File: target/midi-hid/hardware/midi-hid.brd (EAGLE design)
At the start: 100 x 80 mm, 0 parts

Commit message: midi-hid hardware interim drop
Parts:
- added C1, C2: (no value), rcl:C0805
- added D1, D10, D11, D12, D13, D14, D15, D16, D17, D18, D19, D2, D20, D21, D22, D23, D24, D3, D4, D5, D6, D7, D8, D9: (no value), diode:SOD80C
- added IC1: MEGA48/88/168-AU, avr-7:TQFP32-08
- added PAD1, PAD10, PAD11, PAD12, PAD13, PAD14, PAD15, PAD16, PAD17, PAD18, PAD19, PAD2, PAD20, PAD21, PAD22, PAD23, PAD24, PAD25, PAD26, PAD27, PAD28, PAD29, PAD3, PAD30, PAD31, PAD32, PAD33, PAD34, PAD35, PAD36, PAD37, PAD38, PAD39, PAD4, PAD40, PAD41, PAD42, PAD43, PAD44, PAD45, PAD46, PAD47, PAD48, PAD49, PAD5, PAD50, PAD51, PAD52, PAD53, PAD54, PAD55, PAD56, PAD6, PAD7, PAD8, PAD9: (no value), wirepad:1,6/0,8
- added Q1: (no value), crystal:HC49/S
- added R1, R10, R11, R12, R13, R14, R15, R16, R17, R18, R19, R2, R20, R21, R22, R23, R24, R25, R26, R27, R28, R29, R3, R30, R31, R32, R4, R5, R6, R7, R8, R9: (no value), rcl:R0805
- added S1, S2, S3, S4: (no value), switch-omron:B3F-40XX
- added SW1, SW2, SW3, SW4: EC12E_SW, switch-alps:ALPS_EC12E_SW
- added T1, T2, T3, T4: (no value), transistor:SOT23-BEC
- added U$1, U$2, U$3, U$4, U$6, U$7, U$8, U$9: (no value), holes:3,0
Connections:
- new net ADC6: IC1.19
- new net ADC7: IC1.22
- new net BUTROW0: IC1.15
- new net BUTROW1: IC1.16
- new net BUTROW2: IC1.17
- new net COLUMN0: IC1.23
- new net COLUMN1: IC1.24
- new net COLUMN2: IC1.25
- new net COLUMN3: IC1.26
- new net ENCROWA: IC1.12
- new net ENCROWB: IC1.13
- new net ENCROWS: IC1.14
- new net GND: C1.2, C2.2, IC1.21, IC1.3, IC1.5, PAD11.1, PAD17.1, PAD23.1, PAD29.1, PAD35.1, PAD41.1, PAD47.1, PAD53.1
- new net INTOUT: IC1.31
- new net LEDROW0: IC1.32
- new net LEDROW1: IC1.1
- new net LEDROW2: IC1.2
- new net LEDROW3: IC1.9, R3.1
- new net LEDROW4: IC1.10
- new net LEDROW5: IC1.11
- new net LEDROWB: IC1.30
- new net N$10: SW2.D
- new net N$11: D13.C, SW3.B
- new net N$12: D14.C, SW3.A
- new net N$14: D15.C, SW4.B
- new net N$15: D16.C, SW4.A
- new net N$17: SW4.C
- new net N$18: SW4.D
- new net N$19: SW3.C
- new net N$20: SW3.D
- new net N$21: C1.1, IC1.7, Q1.1
- new net N$22: C2.1, IC1.8, Q1.2
- new net N$23: R29.2, T1.B
- new net N$24: PAD36.1, R1.2
- new net N$25: PAD37.1, R2.2
- new net N$26: PAD38.1, R3.2
- new net N$27: R30.2, T2.B
- new net N$28: PAD42.1, R4.2
- new net N$29: PAD43.1, R5.2
- new net N$30: PAD44.1, R6.2
- new net N$31: R31.2, T3.B
- new net N$32: PAD48.1, R7.2
- new net N$33: PAD49.1, R8.2
- new net N$34: PAD50.1, R9.2
- new net N$35: R32.2, T4.B
- new net N$36: PAD54.1, R10.2
- new net N$37: PAD55.1, R11.2
- new net N$38: PAD56.1, R12.2
- new net N$39: PAD33.1
- new net N$4: SW1.C
- new net N$40: D3.A, PAD34.1
- new net N$41: PAD39.1
- new net N$42: D7.A, PAD40.1
- new net N$43: PAD45.1
- new net N$44: D4.A, PAD46.1
- new net N$45: PAD51.1
- new net N$46: D8.A, PAD52.1
- new net N$47: PAD14.1, R15.2
- new net N$48: PAD13.1, R14.2
- new net N$49: PAD12.1, R13.2
- new net N$5: SW1.D
- new net N$51: PAD20.1, R18.2
- new net N$52: PAD19.1, R17.2
- new net N$53: PAD18.1, R16.2
- new net N$54: R2.1
- new net N$55: R1.1
- new net N$56: PAD24.1, R19.2
- new net N$57: PAD25.1, R20.2
- new net N$58: PAD26.1, R21.2
- new net N$59: PAD32.1, R24.2
- new net N$6: D11.C, SW2.B
- new net N$60: PAD31.1, R23.2
- new net N$61: PAD30.1, R22.2
- new net N$62: R7.1
- new net N$63: PAD9.1
- new net N$64: D1.A, PAD10.1
- new net N$65: PAD15.1
- new net N$66: D5.A, PAD16.1
- new net N$67: PAD21.1
- new net N$68: D2.A, PAD22.1
- new net N$69: PAD27.1
- new net N$7: D12.C, SW2.A
- new net N$70: D6.A, PAD28.1
- new net N$71: PAD2.1
- new net N$72: PAD1.1, R28.2
- new net N$73: PAD4.1
- new net N$74: PAD3.1, R27.2
- new net N$75: PAD6.1
- new net N$76: PAD5.1, R26.2
- new net N$77: PAD8.1
- new net N$78: PAD7.1, R25.2
- new net N$79: R8.1
- new net N$80: R9.1
- new net N$81: R12.1
- new net N$82: R11.1
- new net N$83: R10.1
- new net N$84: R6.1
- new net N$85: R5.1
- new net N$86: R4.1
- new net N$9: SW2.C
- new net RESET: IC1.29
- new net SCL: IC1.28
- new net SDA: IC1.27
- new net VCC: IC1.18, IC1.20, IC1.4, IC1.6
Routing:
- net LEDROW3: track 0.00 -> 51.6 mm
- net GND: track 0.00 -> 25.2 mm
- net N$22: track 0.00 -> 6.68 mm
- net N$21: track 0.00 -> 5.02 mm

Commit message: midi-hid hardware interim drop
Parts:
- added U$5: (no value), holes:3,0
- moved R29 27.2 mm to (27.8, 27.0), turned to 90 degrees
- moved R30 27.2 mm to (46.8, 27.0), turned to 90 degrees
- moved R31 26.8 mm to (65.8, 27.0), turned to 90 degrees
- moved R32 26.8 mm to (84.8, 27.0), turned to 90 degrees
- moved T1 26.2 mm to (30.8, 27.0), turned to 270 degrees
- moved T2 26.2 mm to (49.8, 27.0), turned to 270 degrees
- moved T3 26.2 mm to (68.8, 27.0), turned to 270 degrees
- moved T4 26.2 mm to (87.8, 27.0), turned to 270 degrees
- moved D17 19.6 mm to (15.5, 80.5), turned to 0 degrees
- moved D18 19.6 mm to (34.5, 80.5), turned to 0 degrees
- moved D19 19.6 mm to (53.5, 80.5), turned to 0 degrees
- moved D20 19.6 mm to (72.5, 80.5), turned to 0 degrees
- moved D10 16.5 mm to (24.0, 91.5), turned to 270 degrees
- moved D12 16.5 mm to (43.0, 91.5), turned to 270 degrees
- moved D14 16.5 mm to (62.0, 91.5), turned to 270 degrees
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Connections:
- new net C0: D1.C, D3.C, SW1.C, SW1.D, T1.C
- new net C1: D5.C, D7.C, SW2.C, SW2.D, T2.C
- new net C2: D2.C, D4.C, SW3.C, SW3.D, T3.C
- new net C3: D6.C, D8.C, SW4.C, SW4.D, T4.C
- new net N$1: D9.C, SW1.B
- new net N$13: D19.C, SW3.E
- new net N$16: D20.C, SW4.E
- new net N$2: D10.C, SW1.A
- new net N$3: D17.C, SW1.E
- new net N$50: R24.1
- new net N$8: D18.C, SW2.E
- new net N$87: R16.1
- new net N$91: R31.1
- new net N$95: R32.1
- net COLUMN0: now also R29.1
- net COLUMN1: now also R30.1
- net ENCROWA: now also D10.A, D12.A, D14.A, D16.A
- net ENCROWB: now also D11.A, D13.A, D15.A, D9.A
- net ENCROWS: now also D17.A, D18.A, D19.A, D20.A
- net GND: now also T1.E, T2.E, T3.E, T4.E
- net LEDROW4: now also R2.1
- net LEDROW5: now also R1.1
- net N$10: now also R19.1; no longer SW2.D
- net N$17: now also R20.1; no longer SW4.C
- net N$18: now also R21.1; no longer SW4.D
- net N$19: now also R22.1; no longer SW3.C
- net N$20: now also R23.1; no longer SW3.D
- net N$4: now also R13.1; no longer SW1.C
- net N$5: now also R14.1; no longer SW1.D
- net N$54: now also R18.1; no longer R2.1
- net N$55: now also R17.1; no longer R1.1
- net N$9: now also R15.1; no longer SW2.C
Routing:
- net ENCROWB: track 0.00 -> 138.9 mm
- net ENCROWA: track 0.00 -> 134.2 mm
- net ENCROWS: track 0.00 -> 134.1 mm
- net C1: track 0.00 -> 95.4 mm
- net C0: track 0.00 -> 92.5 mm
- net C3: track 0.00 -> 92.5 mm
- net C2: track 0.00 -> 92.5 mm
- net LEDROW3: track 51.6 -> 0.77 mm
- net N$6: track 0.00 -> 3.30 mm
- net N$14: track 0.00 -> 3.30 mm
- net N$11: track 0.00 -> 3.30 mm
- net N$1: track 0.00 -> 3.30 mm
- net N$70: track 0.00 -> 2.30 mm
- net N$68: track 0.00 -> 2.30 mm
- net N$66: track 0.00 -> 2.30 mm
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
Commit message: routing midi-hid
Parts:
- added C3, C4: (no value), rcl:C0805
- added C5: (no value), rcl:E2,5-6
- added PAD57, PAD58, PAD59: WIREPAD1,6/0,8, wirepad:1,6/0,8
- added R33, R34: (no value), rcl:0207/10
- added SV1: (no value), con-lstb:MA05-1
- added USBCONN: MICRO-USB, microusb:MICRO-USB
- moved R12 6.95 mm to (75.5, 77.0), turned to 0 degrees
- moved R15 6.95 mm to (18.5, 52.0), turned to 0 degrees
- moved R18 6.95 mm to (37.5, 52.0), turned to 0 degrees
- moved R24 6.95 mm to (75.5, 52.0), turned to 0 degrees
- moved R3 6.95 mm to (18.5, 77.0), turned to 0 degrees
- moved R6 6.95 mm to (37.5, 77.0), turned to 0 degrees
- moved R9 6.95 mm to (56.5, 77.0), turned to 0 degrees
- moved R11 4.27 mm to (75.5, 75.0), turned to 0 degrees
- moved R14 4.27 mm to (18.5, 50.0), turned to 0 degrees
- moved R17 4.27 mm to (37.5, 50.0), turned to 0 degrees
- moved R2 4.27 mm to (18.5, 75.0), turned to 0 degrees
- moved R23 4.27 mm to (75.5, 50.0), turned to 0 degrees
- moved R5 4.27 mm to (37.5, 75.0), turned to 0 degrees
- moved R8 4.27 mm to (56.5, 75.0), turned to 0 degrees
- moved R25 3.61 mm to (81.5, 20.0), turned to 180 degrees
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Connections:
- removed net N$10: R19.1
- removed net N$17: R20.1
- removed net N$18: R21.1
- removed net N$19: R22.1
- removed net N$20: R23.1
- removed net N$39: PAD33.1
- removed net N$4: R13.1
- removed net N$41: PAD39.1
- removed net N$43: PAD45.1
- removed net N$45: PAD51.1
- removed net N$5: R14.1
- removed net N$50: R24.1
- removed net N$54: R18.1
- removed net N$55: R17.1
- removed net N$62: R7.1
- removed net N$63: PAD9.1
- removed net N$65: PAD15.1
- removed net N$67: PAD21.1
- removed net N$69: PAD27.1
- removed net N$71: PAD2.1
- removed net N$73: PAD4.1
- removed net N$75: PAD6.1
- removed net N$77: PAD8.1
- removed net N$79: R8.1
- removed net N$80: R9.1
- removed net N$81: R12.1
- removed net N$82: R11.1
- removed net N$83: R10.1
- removed net N$84: R6.1
- removed net N$85: R5.1
- removed net N$86: R4.1
- removed net N$87: R16.1
- removed net N$9: R15.1
- removed net N$95: R32.1
- new net DM: USBCONN.2
- new net DP: USBCONN.3
- new net ID: USBCONN.4
- new net N$88: D22.C, S2.2
- new net N$89: D21.C, S1.2
- new net N$90: D23.C, S3.2
- net ADC6: now also PAD58.1
- net ADC7: now also PAD59.1
- net BUTROW0: now also PAD33.1, PAD39.1, PAD45.1, PAD51.1
- net BUTROW1: now also PAD15.1, PAD21.1, PAD27.1, PAD9.1
- net BUTROW2: now also D21.A, D22.A, D23.A, D24.A
- net C0: now also PAD2.1, S1.4
- net C1: now also PAD4.1, S2.4
- net C2: now also PAD6.1, S3.4
- net C3: now also PAD8.1, S4.4
- net COLUMN2: now also R31.1
- net COLUMN3: now also R32.1
- net GND: now also C3.2, C4.2, C5.-, SV1.2, USBCONN.5, USBCONN.GND1, USBCONN.GND2
- net INTOUT: now also SV1.5
- net LEDROW0: now also R15.1, R18.1, R21.1, R24.1
- net LEDROW1: now also R14.1, R17.1, R20.1, R23.1
- net LEDROW2: now also R13.1, R16.1, R19.1, R22.1
- net LEDROW3: now also R12.1, R6.1, R9.1
- net LEDROW4: now also R11.1, R5.1, R8.1
- net LEDROW5: now also R10.1, R4.1, R7.1
- net LEDROWB: now also R25.1, R26.1, R27.1, R28.1
- net N$91: now also D24.C, S4.2; no longer R31.1
- net RESET: now also PAD57.1
- net SCL: now also SV1.3
- net SDA: now also SV1.4
- net VCC: now also C3.1, C4.1, C5.+, SV1.1, USBCONN.1
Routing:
- net GND: track 25.2 -> 580.6 mm, vias 0 -> 4
- net VCC: track 0.00 -> 349.0 mm, vias 0 -> 1
- net INTOUT: track 0.00 -> 131.6 mm
- net LEDROW3: track 0.77 -> 122.5 mm, vias 0 -> 5
- net LEDROW4: track 0.78 -> 119.3 mm, vias 0 -> 5
- net LEDROW0: track 0.00 -> 118.2 mm, vias 0 -> 5
- net LEDROW5: track 0.78 -> 116.2 mm, vias 0 -> 5
- net LEDROW1: track 0.00 -> 110.1 mm, vias 0 -> 5
- net LEDROW2: track 0.00 -> 108.0 mm, vias 0 -> 5
- net SDA: track 0.00 -> 97.7 mm, vias 0 -> 2
- net SCL: track 0.00 -> 94.9 mm, vias 0 -> 2
- net BUTROW2: track 0.00 -> 93.6 mm, vias 0 -> 5
- net LEDROWB: track 0.00 -> 93.3 mm, vias 0 -> 5
- net BUTROW0: track 0.00 -> 93.2 mm
- net BUTROW1: track 0.00 -> 78.3 mm
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
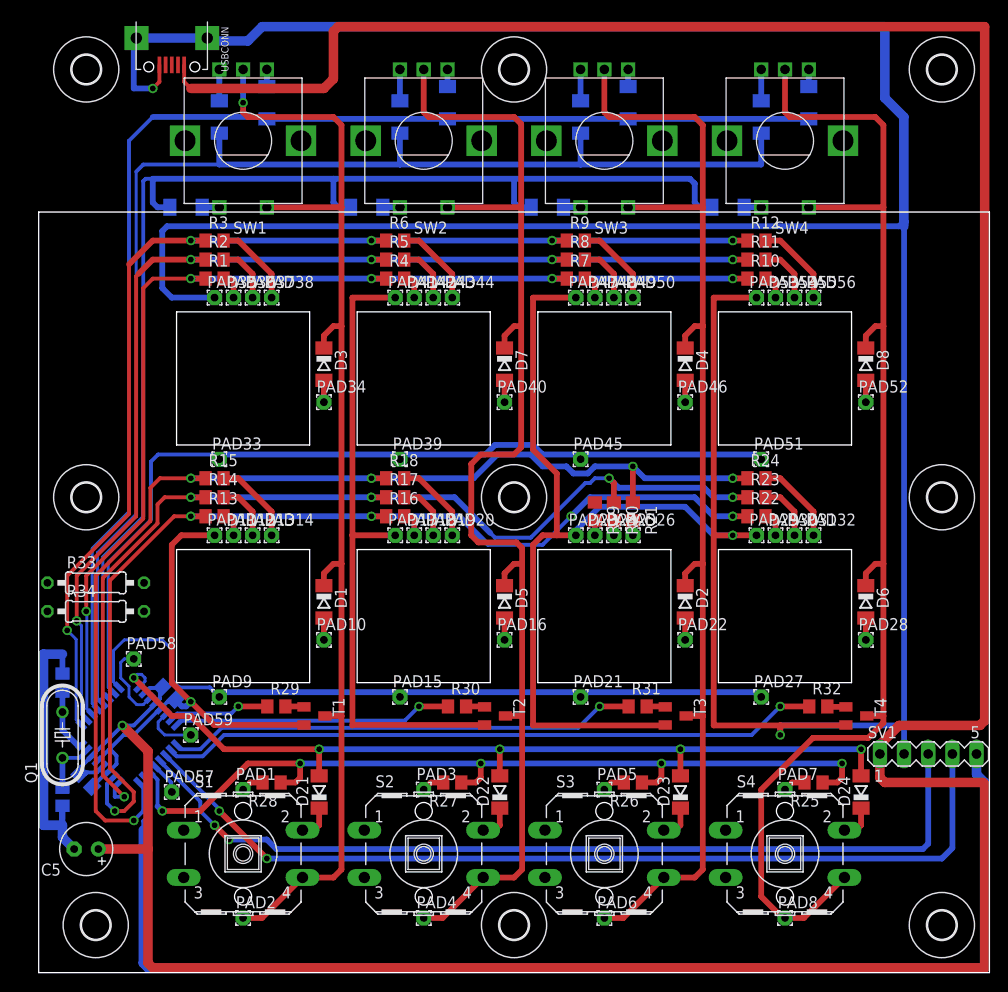
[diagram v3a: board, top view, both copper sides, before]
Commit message: midi-hid hardware
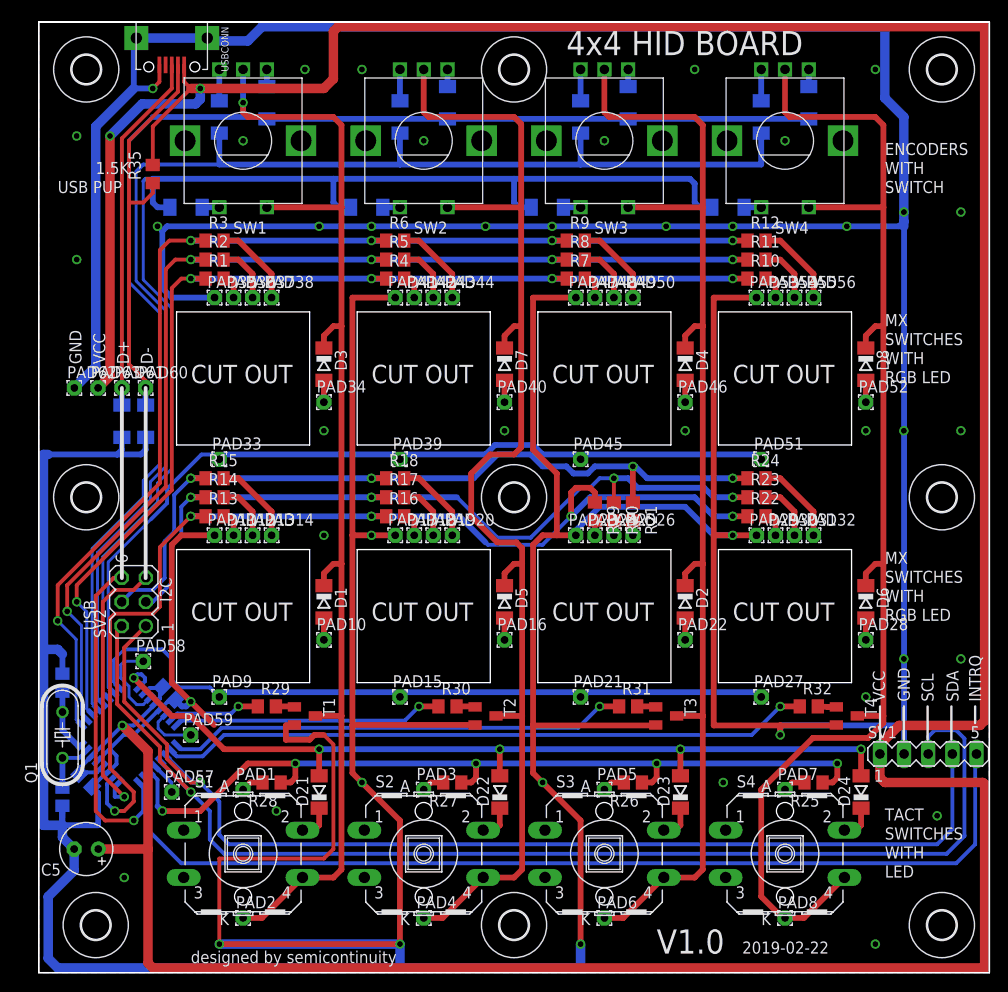
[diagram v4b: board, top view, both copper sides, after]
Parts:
- removed R33, R34: (no value), rcl:0207/10
- added D25, D26: (no value), diode:SOD80C
- added PAD60, PAD61, PAD62, PAD63: (no value), wirepad:1,6/0,8
- added R35: 1.5k, rcl:R0805
- added SV2: (no value), con-lstb:MA03-2
- moved PAD58 1.03 mm to (11.0, 32.8)
- moved R29 1.00 mm to (24.0, 28.0)
- moved R30 1.00 mm to (43.0, 28.0)
- moved R31 1.00 mm to (62.0, 28.0)
- moved R32 1.00 mm to (81.0, 28.0)
- moved T1 1.00 mm to (28.0, 27.0)
- moved T2 1.00 mm to (47.0, 27.0)
- moved T3 1.00 mm to (66.0, 27.0)
- moved T4 1.00 mm to (85.0, 27.0)
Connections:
- new net LR0: R15.1, R18.1, R21.1, R24.1, SV2.4
- new net LR1: R14.1, R17.1, R20.1, R23.1, SV2.3
- net DM: now also D26.C, PAD60.1, R35.1
- net DP: now also D25.C, PAD61.1
- net GND: now also D25.A, D26.A, PAD62.1
- net LEDROW0: now also SV2.6; no longer R15.1, R18.1, R21.1, R24.1
- net LEDROW1: now also SV2.5; no longer R14.1, R17.1, R20.1, R23.1
- net SCL: now also SV2.2
- net SDA: now also SV2.1
- net VCC: now also PAD63.1, R35.2
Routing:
- net GND: track 580.6 -> 848.4 mm, vias 4 -> 42
- net LR0: track 0.00 -> 85.3 mm, vias 0 -> 4
- net LEDROW0: track 118.2 -> 35.1 mm, vias 5 -> 1
- net LR1: track 0.00 -> 82.8 mm, vias 0 -> 4
- net LEDROW1: track 110.1 -> 29.7 mm, vias 5 -> 1
- net VCC: track 349.0 -> 397.9 mm, vias 1 -> 3
- net DM: track 0.00 -> 42.6 mm
- net DP: track 0.00 -> 37.9 mm
- net SCL: track 94.9 -> 128.6 mm, vias 2 -> 1
- net INTOUT: track 131.6 -> 104.5 mm
- net SDA: track 97.7 -> 118.5 mm, vias 2 -> 1
- net LEDROW2: track 108.0 -> 115.7 mm
- net ENCROWA: track 134.2 -> 136.9 mm
- net BUTROW0: track 93.2 -> 90.5 mm
- net ENCROWB: track 137.1 -> 139.7 mm
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- added copper zone on layer 1, net GND
- added copper zone on layer 16, net GND
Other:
- board size 100 x 80 mm -> 100 x 100 mm
- board text added: "1.5K"
- board text added: "2019-02-22"
- board text added: "4x4 HID BOARD"
- board text added: "A"
- board text added: "ADC6"
- board text added: "ADC7"
- board text added: "CUT OUT"
- board text added: "D+"
- board text added: "D-"
- board text added: "ENCODERS"
- board text added: "FOR"
- board text added: "GND"
- board text added: "I2C"
- board text added: "INTRQ"
- board text added: "K"
- board text added: "LED"
- board text added: "MISO"
- board text added: "MOSI"
- board text added: "MX"
- board text added: "RESET"
- board text added: "RGB LED"
- board text added: "SCK"
- board text added: "SCL"
- board text added: "SDA"
- board text added: "SWITCH"
- board text added: "SWITCHES"
- board text added: "TACT"
- board text added: "USB"
- board text added: "USB PUP"
- board text added: "V1.0"
- board text added: "VCC"
- board text added: "WITH"
- board text added: "ZENER"
- board text added: "designed by semicontinuity"
